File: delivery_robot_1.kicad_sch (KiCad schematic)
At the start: 23 parts, among them J1 SWD, J2 XT30PW-M, J4 BOOT0 jumper, SW1 RESET, U1 STM32F091RCTx, Y3 8MHz

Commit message: Rename power nets, add mounting holes, retitle sheet 1, clear ERC
Power nets, no commas, named by function:
- "+5V, 2A" -> +5V_SYS, "+5V, 6A PI" -> +5V_PI, "+5V, 6A AUX" -> +5V_AUX
Buck sheets renamed to Buck 5V SYS / Buck 5V PI / Buck 5V AUX. Notes,
descriptions, README and docs updated.

Mechanical and title:
- H1-H4: M3 mounting holes, 3.2 mm plated, isolated (no net), not in BOM
- Sheet 1 title: "Delivery Robot Main Board"

ERC, now 0 errors and 0 warnings (was 4 errors, 15 warnings):
- PWR_FLAGs on +12V (after F1), GND (at J2), +3.3VA (after FB2) and
  +5V_SYS (after the TPS54202's L1)
- TPSM63606 symbol pin types set (VOUT power out, FB/EN input, VIN/
  VLDOIN/GND power in, PG open collector, others passive) in both buck
  sheets and libs/TPSM63606RDLR.kicad_sym
- U1 STM32F091RCTx and Y3 Crystal_GND24 moved to a new
  libs/project_symbols.kicad_sym holding the versions this design uses
  (the current KiCad library moved their pins); libs/TPS54202DDCR made
  to match the schematic's U3
Connectivity unchanged: same 108 nets and pins.

Co-Authored-By: Claude Opus 5.5 <noreply@anthropic.com>
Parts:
- added H1, H2, H3, H4: M3, MountingHole:MountingHole_3.2mm_M3_Pad, symbol Mechanical:MountingHole
- U1: symbol MCU_ST_STM32F0:STM32F091RCTx -> project_symbols:STM32F091RCTx
- Y3: symbol Device:Crystal_GND24 -> project_symbols:Crystal_GND24
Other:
- sheet Buck 12V-5V 2A renamed Buck 5V SYS
- sheet Buck 12V-5V 6A AUX renamed Buck 5V AUX
- sheet Buck 12V-5V 6A PI renamed Buck 5V PI
- note added: "12 V to 5 V / 6 A buck - U2 (TPSM63606) Output is the +5V_PI net (feeds the Pi via F2/J14)"
- note added: "Mounting holes - 4x M3 (3.2 mm plated, isolated, not on GND). Place one per board corner; not in the BOM (no part to buy)."
- note removed: "12 V to 5 V / 6 A buck - U2 (TPSM63606) Output is the +5V, 6A PI net (feeds the Pi via F2/J14)"
- title: STM32F091RC core - ready for peripherals -> Delivery Robot Main Board

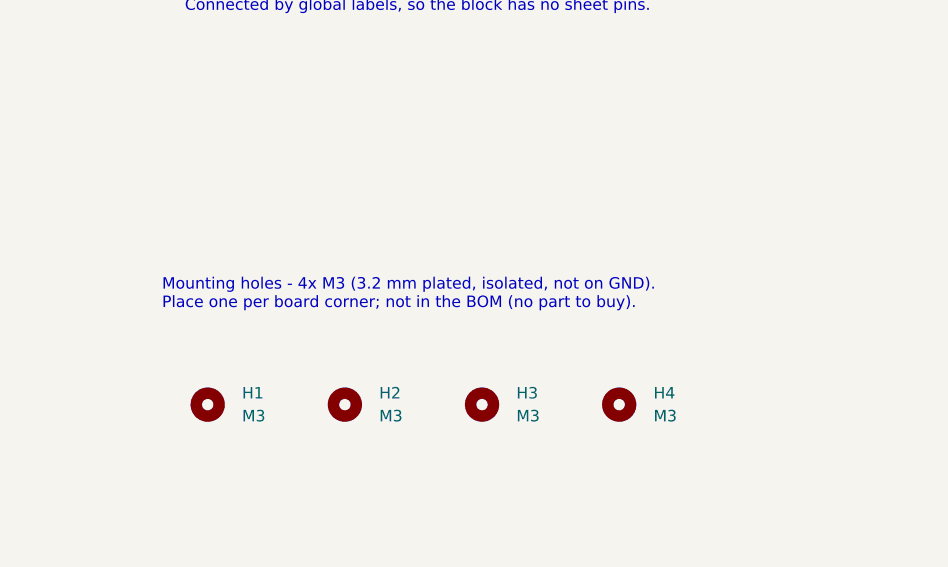
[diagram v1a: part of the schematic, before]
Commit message: Start PCB layout: place and lock M3 mounting holes with keepouts
Add delivery_robot_1.kicad_pcb (80 x 90 mm outline, 4-layer stackup
with In1.Cu GND and In2.Cu PWR, all footprints imported).

Mounting holes H1-H4, 4 mm in from each corner of the outline (top-left
corner at 85, 50 mm):
  H1 (4, 4)   H2 (76, 4)   H3 (4, 86)   H4 (76, 86) mm
- Footprint changed to MountingHole_3.2mm_M3: non-plated (NPTH), no
  copper ring, no pad number. Updated in the schematic and swapped in
  place on the board; DRC schematic parity is clean.
- All four footprints locked.
- A 7 x 7 mm keepout rule area centred on each hole on F.Cu, In1.Cu,
  In2.Cu and B.Cu: no tracks, vias or copper fills; pads and footprints
  allowed so the hole itself is not flagged.
- H1/H2 reference text moved below the hole so it stays on the board.

Schematic: H1-H4 footprint, descriptions and mounting-hole note
updated for NPTH, plus KiCad's re-save of the sheet.

Co-Authored-By: Claude Opus 5.5 <noreply@anthropic.com>
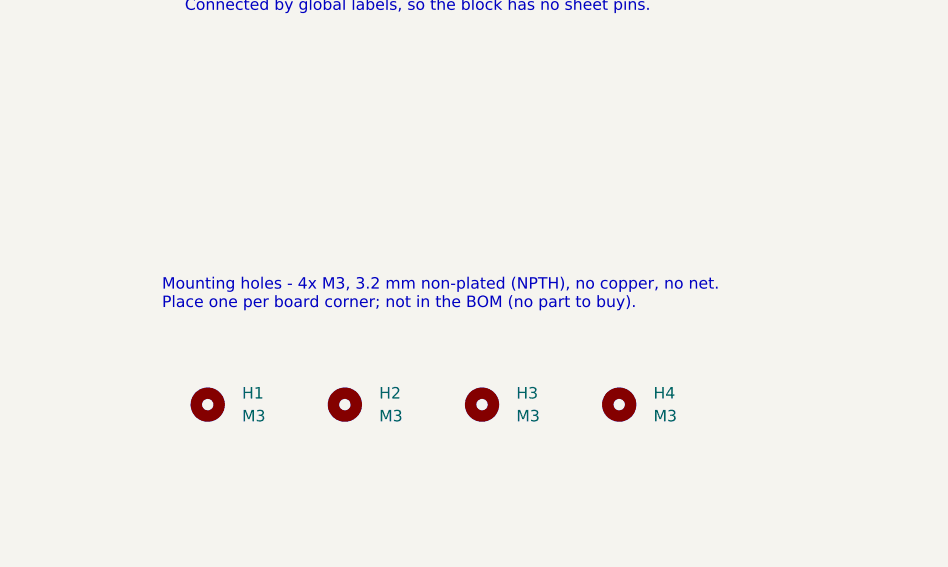
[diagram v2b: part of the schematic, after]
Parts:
- H1, H2, H3, H4: footprint MountingHole:MountingHole_3.2mm_M3_Pad -> MountingHole:MountingHole_3.2mm_M3
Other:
- note added: "Mounting holes - 4x M3, 3.2 mm non-plated (NPTH), no copper, no net. Place one per board corner; not in the BOM (no part to buy)."
- note removed: "Mounting holes - 4x M3 (3.2 mm plated, isolated, not on GND). Place one per board corner; not in the BOM (no part to buy)."

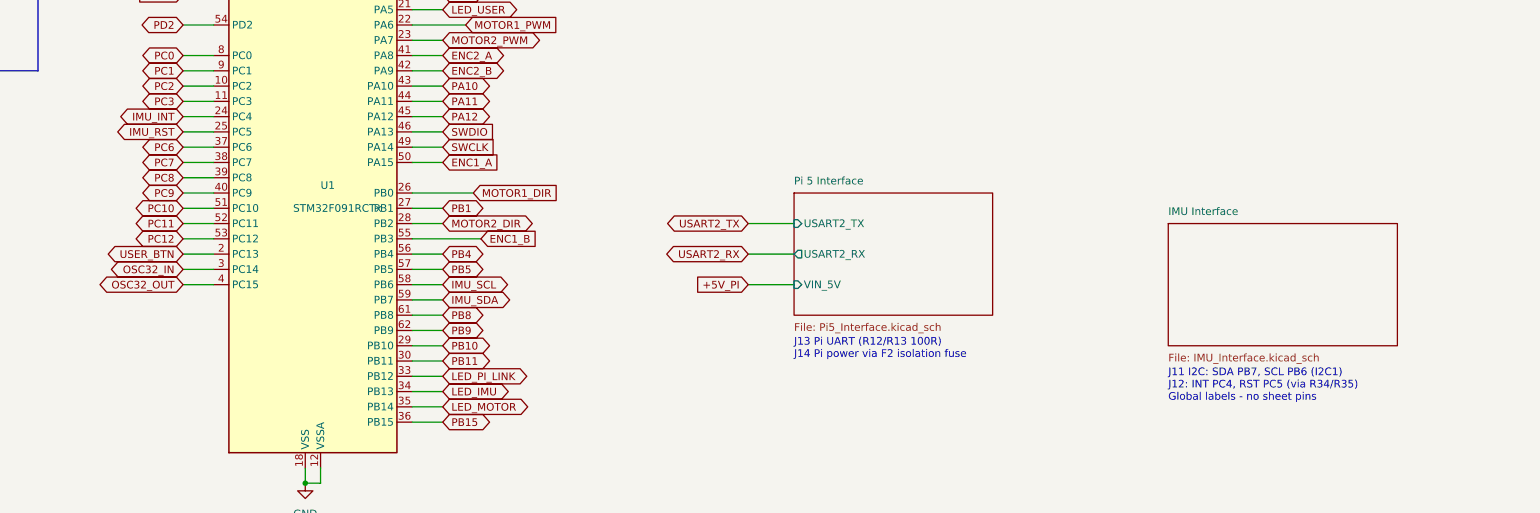
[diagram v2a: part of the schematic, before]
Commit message: Remove the IMU from the board; it will be wired off-board
The BNO085 IMU is now connected discretely off the PCB, so everything
for it is removed from the schematic and the layout:
- Delete the IMU Interface sheet (IMU_Interface.kicad_sch): J11 STEMMA
  QT connector, J12 INT/RST header, DNP I2C pull-ups R10/R11 and series
  resistors R34/R35; remove its sheet block, note and project entry
- Remove debug LED D10 / R23 (LED_IMU on PB13)
- Rename the freed MCU nets back to plain pins, still broken out on the
  GPIO headers: IMU_SCL -> PB6, IMU_SDA -> PB7 (J9), IMU_INT -> PC4,
  IMU_RST -> PC5 (J10), LED_IMU -> PB13 (J9)
- Drop IMU wiring notes and the IMU 3.3 V budget line from the LDO sheet;
  update the J9/J10 pin descriptions, debug-LED note and README

Board updated to match (as Update PCB from Schematic): the eight
unplaced footprints deleted, pad nets renamed, J9/J10 descriptions
synced. ERC 0; DRC unchanged at 57 with 276 unrouted (was 293);
schematic parity clean.

Co-Authored-By: Claude Opus 5.5 <noreply@anthropic.com>
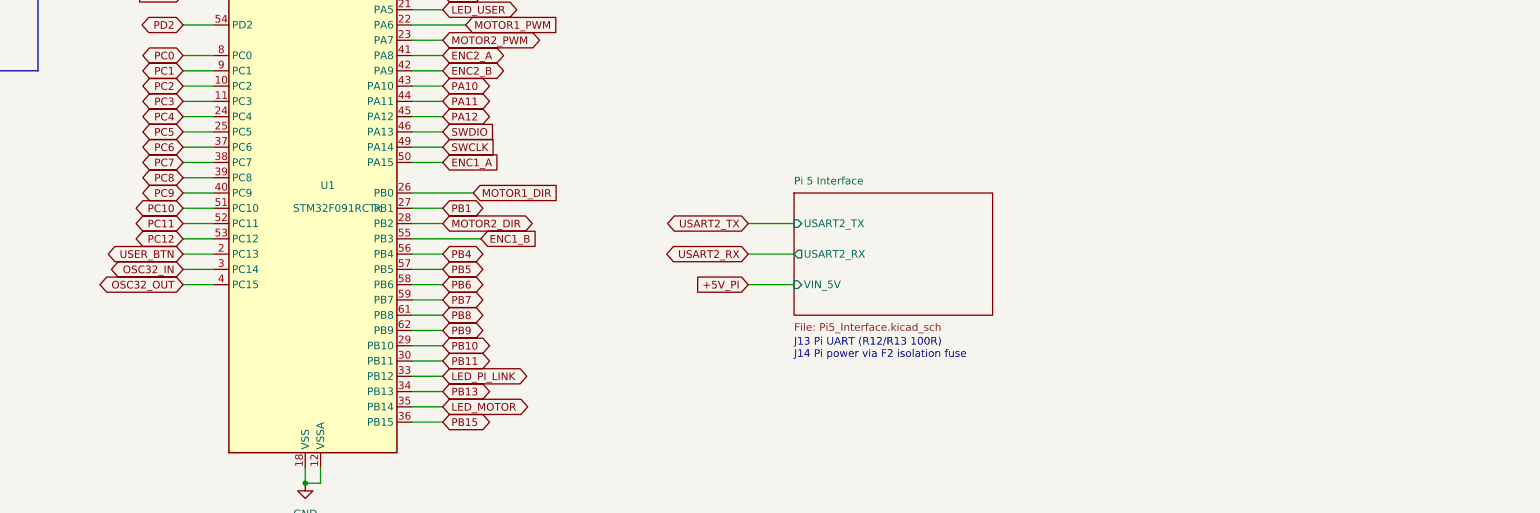
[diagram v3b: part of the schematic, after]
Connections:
- net IMU_INT renamed PC4
- net IMU_RST renamed PC5
- net IMU_SCL renamed PB6
- net IMU_SDA renamed PB7
- net LED_IMU renamed PB13
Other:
- removed sheet IMU Interface
- note removed: "J11 I2C: SDA PB7, SCL PB6 (I2C1) J12: INT PC4, RST PC5 (via R34/R35) Global labels - no sheet pins"
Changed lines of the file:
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@@
 		)
 	)
-	(text "J11 I2C: SDA PB7, SCL PB6 (I2C1)\nJ12: INT PC4, RST PC5 (via R34/R35)\nGlobal labels - no sheet pins"
-		(exclude_from_sim no)
-		(at 339.09 194.31 0)
-		(effects
-			(font
-				(size 1.27 1.27)
-			)
-			(justify left top)
-		)
-	)
 	(text "Jumper open = run from flash \nJumper fitted + reset = ROM bootloader "
 		(exclude_from_sim no)
@@
 		)
 	)
-	(global_label "LED_IMU"
+	(global_label "PB13"
 		(shape bidirectional)
 		(at 218.44 198.12 0)
@@
 		)
 	)
-	(global_label "IMU_SDA"
+	(global_label "PB7"
 		(shape bidirectional)
 		(at 218.44 182.88 0)
@@
 		)
 	)
-	(global_label "IMU_INT"
+	(global_label "PC4"
 		(shape bidirectional)
 		(at 175.26 152.4 180)
@@
 		)
 	)
-	(global_label "IMU_RST"
+	(global_label "PC5"
 		(shape bidirectional)
 		(at 175.26 154.94 180)
@@
 		)
 	)
-	(global_label "IMU_SCL"
+	(global_label "PB6"
 		(shape bidirectional)
 		(at 218.44 180.34 0)
@@
 				)
 			)
-		)
-	)
-	(sheet
-		(at 339.09 170.18)
-		(size 38.1 20.32)
-		(exclude_from_sim no)
-		(in_bom yes)
-		(on_board yes)
-		(dnp no)
-		(stroke
-			(width 0)
-			(type solid)
-		)
-		(fill
-			(color 0 0 0 0)
-		)
-		(property "Sheetname" "IMU Interface"
-			(at 339.09 168.91 0)
-			(show_name no)
-			(do_not_autoplace no)
-			(effects
-				(font
-					(size 1.27 1.27)
-				)
-				(justify left bottom)
-			)
-		)
-		(property "Sheetfile" "IMU_Interface.kicad_sch"
-			(at 339.09 191.77 0)
-			(show_name no)
-			(do_not_autoplace no)
-			(effects
-				(font
-					(size 1.27 1.27)
-				)
-				(justify left top)
-			)
-		)
-		(instances
-			(project "delivery_robot_1"
-				(path "/30314d9c-15a8-4a77-8ae4-b5ba12ed5bc4"
-					(page "11")
-				)
-			)

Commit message: Add input protection, AUX ports, servo interface and Pi control
Implements the 2026-10-15 design review decisions in the schematic.
ERC 0 errors, 0 warnings.

New sheets:
- Input Protection: Q1 SQJ409EP reverse-battery P-FET after F1 (D12
  12 V gate clamp, R36), D13 SMBJ16A TVS on +12V, battery sense
  R37/R38/C37 -> VBAT_SENSE on PA0. PWR_FLAG moves to +12V.
- AUX Outputs: four +5V_AUX ports J18-J21 (JST XH 2-pin: Notecard,
  LiDAR, GNSS, IMU), each through a 1.5 A PTC (F4-F7).
- Servo Interface: J17 (GND, VBAT_SERVO via F3 5 A fuse, SERVO_SIG) for
  the Hiwonder HTS-30HS through an external 11.1-12 V buck. U8
  SN74LVC1T45 translates PB10 (USART3 half-duplex) to the 5 V bus,
  PB11 sets direction; R39-R42 pull-ups/series, D14 ESD.

Root sheet:
- F1 output is now VBAT_FUSED; C36 sits on +12V after Q1. J2-F1 net
  named VBAT_IN. F1 7.5 A -> 10 A (0297010.L).
- Y3/C5/C6 fitted (were DNP).
- PA0 -> VBAT_SENSE, PA1 -> PI_3V3_SENSE, PB10 -> SERVO_TX,
  PB11 -> SERVO_DIR. Notes updated (no more F2 / XT30-only text).

Pi 5 Interface:
- J13 -> 6-pin JST XH: TXD, RXD, GND, PI_3V3, PI_RESET, PI_BOOT0.
- PI_3V3 -> D15 -> AUX_EN (U5 enable) and R44/R45 -> PA1.
- PI_RESET -> Q2 DMN63D8L -> NRST (open drain, R46 pull-down).
- PI_BOOT0 -> R47 1k -> BOOT0, for reflashing over USART2.
- R12/R13 100R -> 1k (PA2/PA3 are TTa, 5 mA injection max).
- Remove TP2 (same net as TP1 since F2 was removed).

Buck 5V AUX: U5 EN from AUX_EN (was +12V), R43 100k pull-down, C40,
J22 force-on jumper. Buck 5V SYS: C49 100 nF at U3 VIN/GND.
U2/U5 value TPSM63606RDLR; VCC design note corrected (internal 1 uF,
must stay NC).

Motor Control (now A3):
- U9/U10 74LVC2G17 encoder buffers on +3V3; encoder series R 100R ->
  1k with C43-C46 1 nF; R48-R51 4.7k pull-ups (DNP).
- F8/F9 0.2 A PTC + C47/C48 on each encoder supply (ENC1_5V, ENC2_5V).
- J7/J15 pin order 5V, GND, A, B (matches the am-3651 plug).
- R52/R53 10k pull-downs on both PWM lines (MDD20A brakes on low).
- F10/F11 PTC in series with J6/J16 p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
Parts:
- C5, C6, Y3: now fitted
- F1: value 7.5A / 32VDC -> 10A / 32VDC; AssemblyBOM 1x Keystone 3568 holder + 1x Littelfuse 029707.5L fuse; ord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 -> 1x Keystone 3568 holder + 1x Littelfuse 0297010.L fuse; ord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; FuseMPN 029707.5L -> 0297010.L; Specification MINI holder with 7.5A / 32VDC fuse; 1000A DC interrupt rati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 -> MINI holder with 10A / 32VDC fuse; 1000A DC interrupt ratin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
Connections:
- net +12V: no longer F1.1
- net VBAT_IN: now reaches F1.2, J2.2 (Pin_2)
- net PA0 renamed VBAT_SENSE
- net PA1 renamed PI_3V3_SENSE
- net PB10 renamed SERVO_TX
- net PB11 renamed SERVO_DIR
- new net VBAT_FUSED: F1.1
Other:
- added sheet AUX Outputs (AUX_Outputs.kicad_sch)
- added sheet Input Protection (Input_Protection.kicad_sch)
- added sheet Servo Interface (Servo_Interface.kicad_sch)
- note added: "12 V to 5 V / 6 A buck - U2 (TPSM63606) Output is the +5V_PI net (feeds the Pi via J14)"
- note added: "Input protection (J2 battery) - see the Input Protection sheet J2 XT30 -> VBAT_IN -> F1 10 A MINI fuse -> VBAT_FUSED -> Q1 reverse-battery P-FET -> +12V (D13 SMBJ16A TVS, C36 bulk, battery sense on PA0). C36 is on +12V after Q1, so it is never reverse-biased. Battery harness fuse at the M8 lugs: 15 A."
- note added: "J13 Pi link, 6-pin JST-XH: UART (R12/R13 1k), GND, Pi 3V3 sense, STM32 reset (Q2) and BOOT0 for reflashing over USART2 J14 Pi power (+5V_PI direct, no fuse)"
- note added: "J17 latch servo: fused VBAT, U8 half-duplex UART (PB10/PB11)"
- note added: "J18-J21: four 5 V peripheral ports, one PTC each"
- note added: "Q1 reverse-battery P-FET, D13 TVS, VBAT_SENSE (PA0)"
- note removed: "12 V to 5 V / 6 A buck - U2 (TPSM63606) Output is the +5V_PI net (feeds the Pi via F2/J14)"
- note removed: "Input protection (J2 battery) Reverse polarity: no P-FET - relies on the keyed XT30 (J2). Why: the XT30 housing cannot be mated reversed, and this avoids an extra series part (and its heat) in the 4-8 A input path. Not covered: a harness crimped backwards at the battery M8 lugs. Mitigation: meter-check harness polarity (+ to J2 pin 2) before first power-up and after any harness rework. C36: 220 u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"
- note removed: "J13 Pi UART (R12/R13 100R) J14 Pi power via F2 isolation fuse"
